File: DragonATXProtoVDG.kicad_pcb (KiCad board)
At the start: 4 copper layers, 123.8 x 85.5 mm, 57 parts, among them IC1 74LS273, J3 JTAG, U1 AD724JR, U3 ATF1508AS-10JI84, Y2 4.433618MHz, Y3 100MHz

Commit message: update CPLD
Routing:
- net +5V: track 99.5 -> 104.6 mm
- net /Q5: track 31.5 -> 30.9 mm

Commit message: refine board design
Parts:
- added J1: Conn_Coaxial, Library:Connector_RCA, F.Cu at (71.4, 96.3)
- added TP10: TestPoint_RowResetPulse, TestPoint:TestPoint_Pad_D1.0mm, F.Cu at (101.3, 81.7)
- added TP11: TestPoint_DA0, TestPoint:TestPoint_Pad_D1.0mm, F.Cu at (91.1, 81.0)
- added TP7: TestPoint_ColourClock, TestPoint:TestPoint_Pad_D1.0mm, F.Cu at (84.6, 70.5)
- added TP8: TestPoint_PixelClock, TestPoint:TestPoint_Pad_D1.0mm, F.Cu at (140.6, 53.9)
- added TP9: TestPoint_ReqFormat, TestPoint:TestPoint_Pad_D1.0mm, F.Cu at (87.6, 49.2)
- C15, C5, C6: footprint Capacitor_Tantalum_SMD:CP_EIA-3216-12_Kemet-S -> Capacitor_Tantalum_SMD:CP_EIA-6032-15_Kemet-U
- Y3: footprint Oscillator:Oscillator_SMD_SeikoEpson_SG8002LB-4Pin_5.0x3.2mm_HandSoldering -> Crystal:Crystal_SMD_7050-4Pin_7.0x5.0mm
- moved C15 11.0 mm to (77.7, 96.3)
- moved C5 10.8 mm to (81.5, 96.3)
- moved R3 10.2 mm to (85.3, 103.3), turned to 90 degrees
- moved R1 9.95 mm to (74.8, 97.5), turned to -90 degrees
- moved C6 9.63 mm to (85.3, 96.3)
- moved R2 6.65 mm to (81.5, 103.3), turned to 90 degrees
- moved JP1 6.31 mm to (83.8, 50.9)
- moved R4 6.31 mm to (79.7, 49.9)
- moved C10 4.07 mm to (82.8, 85.9), turned to -90 degrees
- moved C1 2.37 mm to (132.8, 72.9), turned to -45 degrees
- moved C2 2.13 mm to (92.2, 43.0), turned to 135 degrees
- moved C23 1.93 mm to (106.9, 84.0), turned to -135 degrees
- moved C18 1.19 mm to (88.3, 63.4)
- moved Y3 0.74 mm to (91.8, 71.8)
- moved C22 0.40 mm to (99.5, 76.2)
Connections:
- U3 pad 22: unconnected-(U3-I/O-Pad22) -> /DA1
- U3 pad 24: unconnected-(U3-I/O-Pad24) -> /DA2
- U3 pad 25: unconnected-(U3-I/O-Pad25) -> /DA3
- U3 pad 30: unconnected-(U3-I/O-Pad30) -> /DA4
- U3 pad 31: unconnected-(U3-I/O-Pad31) -> /DA5
- U3 pad 35: unconnected-(U3-I/O-Pad35) -> /DA6
- U3 pad 36: unconnected-(U3-I/O-Pad36) -> /DA7
- U3 pad 39: unconnected-(U3-I/O-Pad39) -> /DA8
- U3 pad 40: unconnected-(U3-I/O-Pad40) -> /DA9
- U3 pad 41: unconnected-(U3-I/O-Pad41) -> /DA10
- U3 pad 48: unconnected-(U3-I/O-Pad48) -> /DA11
- U3 pad 49: unconnected-(U3-I/O-Pad49) -> /DA12
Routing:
- net /INV: track 103.5 -> 54.9 mm, vias 4 -> 0
- net /CSS: track 80.1 -> 59.3 mm, vias 2 -> 0
- net /Q7: track 73.1 -> 53.5 mm, vias 2 -> 0
- net /GM2: track 93.3 -> 74.3 mm, vias 2 -> 0
- net /GM1: track 87.9 -> 68.9 mm, vias 2 -> 0
- net /GM0: track 88.3 -> 69.9 mm, vias 2 -> 0
- net /~{A}/G: track 82.7 -> 66.5 mm, vias 2 -> 0
- net Composite: track 9.61 -> 25.4 mm
- net /VCLK: track 103.6 -> 89.0 mm, vias 2 -> 0
- net /~{RP}: track 0.00 -> 13.1 mm
- net Net-(C15-Pad2): track 11.5 -> 3.14 mm
- net Format: track 13.9 -> 20.3 mm
- net Luma: track 17.5 -> 12.7 mm
- net /RAS: track 58.3 -> 54.2 mm
- net Chroma: track 14.7 -> 10.9 mm
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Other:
- board text added: "+5V"
- board text added: "GND"
- board text added: "Test Points TP1 = Blue TP2 = Red TP3 = Green TP4 = Output Format TP7 = Colour Carrier TP8 = Video Clk TP9 = Requested Format TP10 = Ext Char Rom Row Reset TP11 = DA0 C5 = Chroma C6 = Luma C15 = Composite"
- board text added: "use EPM7128SLC84 (Altera/Intel) or ATF1508AS (Atmel/AMD)"
- board text removed: "Test Points TP1 = Blue TP2 = Red TP3 = Green TP4 = Format C5 = Chroma C6 = Luma C15 = Composite"

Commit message: revise for 1.0.7
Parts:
- added C11: 0.1uF, Capacitor_SMD:C_0805_2012Metric_Pad1.18x1.45mm_HandSolder, F.Cu at (70.8, 65.4)
- added C12: 0.1uF, Capacitor_SMD:C_0805_2012Metric_Pad1.18x1.45mm_HandSolder, F.Cu at (68.7, 65.4)
- added C9: 0.1uF, Capacitor_SMD:C_0805_2012Metric_Pad1.18x1.45mm_HandSolder, F.Cu at (72.9, 65.4)
- added R25: 75R, PCM_Resistor_SMD_AKL:R_0805_2012Metric_Pad1.15x1.40mm_HandSolder, F.Cu at (77.4, 53.5)
- added R26: 75R, PCM_Resistor_SMD_AKL:R_0805_2012Metric_Pad1.15x1.40mm_HandSolder, F.Cu at (77.4, 55.5)
- added R27: 75R, PCM_Resistor_SMD_AKL:R_0805_2012Metric_Pad1.15x1.40mm_HandSolder, F.Cu at (77.4, 57.7)
- added R28: 68R, PCM_Resistor_SMD_AKL:R_0805_2012Metric_Pad1.15x1.40mm_HandSolder, F.Cu at (84.5, 77.8)
- added R29: 68R, PCM_Resistor_SMD_AKL:R_0805_2012Metric_Pad1.15x1.40mm_HandSolder, F.Cu at (84.5, 79.8)
- added R30: 68R, PCM_Resistor_SMD_AKL:R_0805_2012Metric_Pad1.15x1.40mm_HandSolder, F.Cu at (91.6, 31.3)
- added R31: 68R, PCM_Resistor_SMD_AKL:R_0805_2012Metric_Pad1.15x1.40mm_HandSolder, F.Cu at (118.2, 28.5)
- added R32: 68R, PCM_Resistor_SMD_AKL:R_0805_2012Metric_Pad1.15x1.40mm_HandSolder, F.Cu at (132.7, 31.9)
- added R33: 150R, PCM_Resistor_SMD_AKL:R_0805_2012Metric_Pad1.15x1.40mm_HandSolder, F.Cu at (68.7, 50.2)
- added R34: 150R, PCM_Resistor_SMD_AKL:R_0805_2012Metric_Pad1.15x1.40mm_HandSolder, F.Cu at (70.8, 50.2)
- added R35: 150R, PCM_Resistor_SMD_AKL:R_0805_2012Metric_Pad1.15x1.40mm_HandSolder, F.Cu at (72.9, 50.2)
- moved TP2 4.23 mm to (88.3, 31.3)
- moved TP3 0.31 mm to (114.4, 28.5)
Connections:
- R12 pad 2: GREEN -> Net-(R12-Pad2)
- R16 pad 1: GREEN -> Net-(R12-Pad2)
- R18 pad 2: BLUE -> Net-(R18-Pad2)
- R22 pad 1: BLUE -> Net-(R18-Pad2)
- R5 pad 1: RED -> Net-(R30-Pad2)
- R8 pad 2: RED -> Net-(R30-Pad2)
- U1 pad 15: /~{FS} -> Net-(U1-VSYNC)
- U1 pad 16: /~{HS} -> Net-(U1-HSYNC)
- U1 pad 6: RED -> Net-(U1-RED)
- U1 pad 7: GREEN -> Net-(U1-GREEN)
- U1 pad 8: BLUE -> Net-(U1-BLUE)
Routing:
- net GREEN: track 94.6 -> 61.9 mm
- net RED: track 60.3 -> 31.0 mm
- net BLUE: track 108.3 -> 83.2 mm
- net Net-(C12-Pad1): track 0.00 -> 20.9 mm, vias 0 -> 2
- net Net-(C11-Pad1): track 0.00 -> 18.7 mm, vias 0 -> 2
- net Net-(R12-Pad2): track 0.00 -> 17.7 mm
- net Net-(C9-Pad1): track 0.00 -> 16.6 mm
- net Net-(R18-Pad2): track 0.00 -> 13.2 mm
- net Net-(R30-Pad2): track 0.00 -> 12.7 mm
- net /~{FS}: track 96.7 -> 89.4 mm
- net Net-(U1-BLUE): track 0.00 -> 6.87 mm
- net Net-(U1-GREEN): track 0.00 -> 5.99 mm
- net Net-(U1-VSYNC): track 0.00 -> 5.27 mm
- net Net-(U1-RED): track 0.00 -> 4.83 mm
- net /~{HS}: track 65.9 -> 61.5 mm
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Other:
- board text added: "Revision 1.0.7"
- board text removed: "Revision 1.0.2"

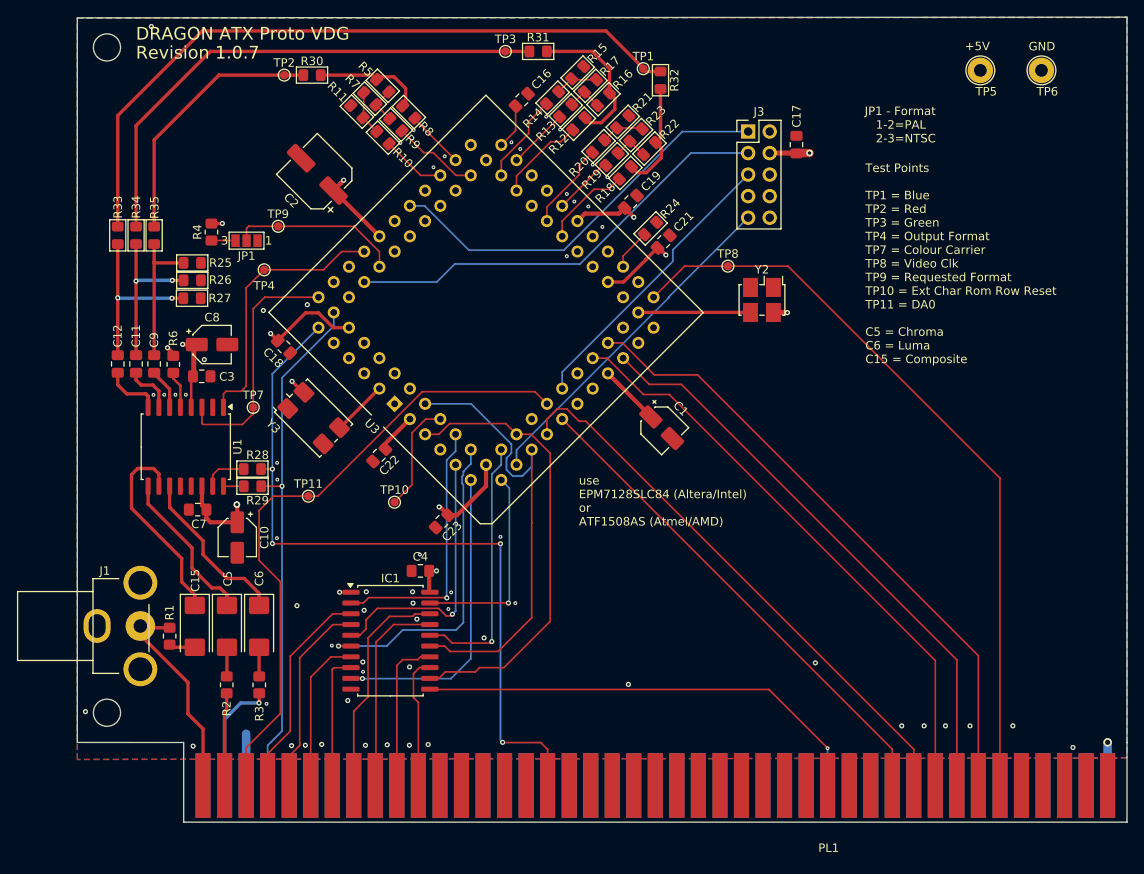
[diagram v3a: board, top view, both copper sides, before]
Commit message: redesign for character rom
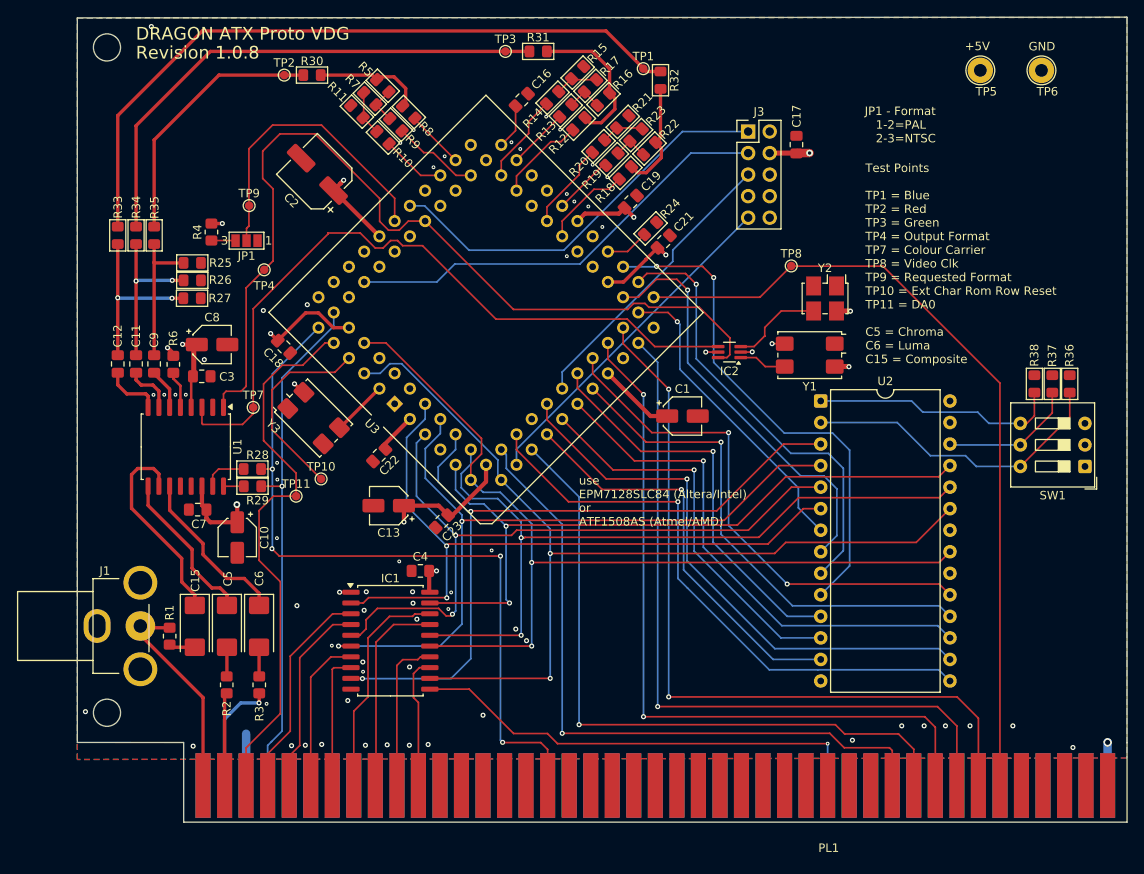
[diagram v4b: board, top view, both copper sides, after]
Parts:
- added C13: 1uF, Capacitor_SMD:CP_Elec_4x4.5, F.Cu at (100.6, 82.1)
- added IC2: 74LVC1G157GW, Package_TO_SOT_SMD:SOT-363_SC-70-6_Handsoldering, F.Cu at (140.8, 64.0)
- added R36: 4K7, PCM_Resistor_SMD_AKL:R_0805_2012Metric_Pad1.15x1.40mm_HandSolder, F.Cu at (180.9, 67.8)
- added R37: 4K7, PCM_Resistor_SMD_AKL:R_0805_2012Metric_Pad1.15x1.40mm_HandSolder, F.Cu at (178.9, 67.8)
- added R38: 4K7, PCM_Resistor_SMD_AKL:R_0805_2012Metric_Pad1.15x1.40mm_HandSolder, F.Cu at (176.8, 67.8)
- added SW1: font, Button_Switch_THT:SW_DIP_SPSTx03_Slide_9.78x9.8mm_W7.62mm_P2.54mm, F.Cu at (182.7, 77.5)
- added U2: 28C256, Package_DIP:DIP-28_W15.24mm, F.Cu at (151.6, 69.8)
- added Y1: 3.579545MHz, Crystal:Crystal_SMD_7050-4Pin_7.0x5.0mm, F.Cu at (150.3, 64.4)
- moved TP10 9.09 mm to (92.6, 79.0)
- moved TP8 7.47 mm to (148.1, 53.8)
- moved Y2 7.44 mm to (152.1, 57.7)
- moved TP9 4.21 mm to (84.2, 46.7)
- moved C1 2.82 mm to (135.3, 71.6), turned to 0 degrees
- moved TP11 1.45 mm to (89.7, 81.0)
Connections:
- U3 pad 10: /Q2 -> /Q5
- U3 pad 11: /Q3 -> /INV
- U3 pad 12: /Q4 -> /Q7
- U3 pad 15: /Q5 -> /CSS
- U3 pad 16: /INV -> /~{A}/G
- U3 pad 17: /Q7 -> /AD3
- U3 pad 18: /~{A}/G -> /AD2
- U3 pad 20: /CSS -> /AD1
- U3 pad 21: /DA0 -> /AD4
- U3 pad 22: /DA1 -> /AD5
- U3 pad 24: /DA2 -> /AD6
- U3 pad 25: /DA3 -> /AD0
- U3 pad 27: /GM0 -> /AD7
- U3 pad 28: /GM1 -> unconnected-(U3-I/O-Pad28)
- U3 pad 29: /GM2 -> /GM0
- U3 pad 30: /DA4 -> /GM1
- U3 pad 31: /DA5 -> /GM2
- U3 pad 34: PALClock -> /AR3
- U3 pad 35: /DA6 -> /AR1
- U3 pad 36: /DA7 -> /AR2
- U3 pad 37: /~{I}/E -> /AR0
- U3 pad 39: /DA8 -> /~{I}/E
- U3 pad 4: /INV -> /Q0
- U3 pad 40: /DA9 -> unconnected-(U3-I/O-Pad40)
- U3 pad 41: /DA10 -> unconnected-(U3-I/O-Pad41)
- U3 pad 48: /DA11 -> unconnected-(U3-I/O-Pad48)
- U3 pad 49: /DA12 -> unconnected-(U3-I/O-Pad49)
- U3 pad 5: /Q7 -> /Q1
- U3 pad 6: /~{RP} -> /Q2
- U3 pad 63: unconnected-(U3-I/O-Pad63) -> FrmFormat
- U3 pad 64: unconnected-(U3-I/O-Pad64) -> Format
- U3 pad 68: FrmFormat -> unconnected-(U3-I/O-Pad68)
- U3 pad 69: Format -> unconnected-(U3-I/O-Pad69)
- U3 pad 74: FMT_CLOCK -> unconnected-(U3-I/O-Pad74)
- U3 pad 77: unconnected-(U3-I/O-Pad77) -> /DA0
- U3 pad 79: unconnected-(U3-I/O-Pad79) -> /~{RP}
- U3 pad 8: /Q0 -> /Q3
- U3 pad 80: unconnected-(U3-I/O-Pad80) -> /INV
- U3 pad 81: unconnected-(U3-I/O/GCLK3-Pad81) -> /Q7
- U3 pad 9: /Q1 -> /Q4
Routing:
- net FrmFormat: track 31.9 -> 106.6 mm
- net /AD3: track 0.00 -> 69.5 mm, vias 0 -> 1
- net /AD4: track 0.00 -> 66.8 mm, vias 0 -> 1
- net /AD5: track 0.00 -> 61.3 mm, vias 0 -> 1
- net /AD7: track 0.00 -> 61.2 mm, vias 0 -> 2
- net /Q4: track 24.2 -> 84.6 mm, vias 1 -> 2
- net /AR0: track 0.00 -> 60.0 mm, vias 0 -> 2
- net /Q5: track 30.9 -> 90.9 mm, vias 1 -> 2
- net /AD6: track 0.00 -> 59.6 mm, vias 0 -> 1
- net /Q7: track 53.5 -> 112.8 mm, vias 0 -> 2
- net FMT_CLOCK: track 29.2 -> 85.8 mm
- net /INV: track 54.9 -> 109.5 mm, vias 0 -> 2
- net /AR1: track 0.00 -> 52.7 mm, vias 0 -> 1
- net /Q3: track 36.2 -> 88.8 mm, vias 1 -> 2
- net /Q0: track 31.3 -> 83.3 mm, vias 1 -> 2
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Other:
- board text added: "Revision 1.0.8"
- board text removed: "Revision 1.0.7"
